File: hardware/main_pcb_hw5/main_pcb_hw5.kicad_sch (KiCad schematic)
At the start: 27 parts, among them J1 MEGA TOP, J10 GBA_Slot, J2 MEGA BOTTOM, J3 CART SLOT TOP ROW, J4 CART SLOT BOTTOM ROW, J5 MEGA SIDE, J6 5V USB, J7 Conn_01x07, J8 EXP2, J9 EXP1, M2_1 Screw_Terminal_01x01, M2_2 Screw_Terminal_01x01, M2_3 Screw_Terminal_01x01, M2_4 Screw_Terminal_01x01, M2_5 Screw_Terminal_01x01, M2_6 Screw_Terminal_01x01, M2_7 Screw_Terminal_01x01, M2_8 Screw_Terminal_01x01, M2_9 Screw_Terminal_01x01, SW1 VOLTAGE, SW2 POWER

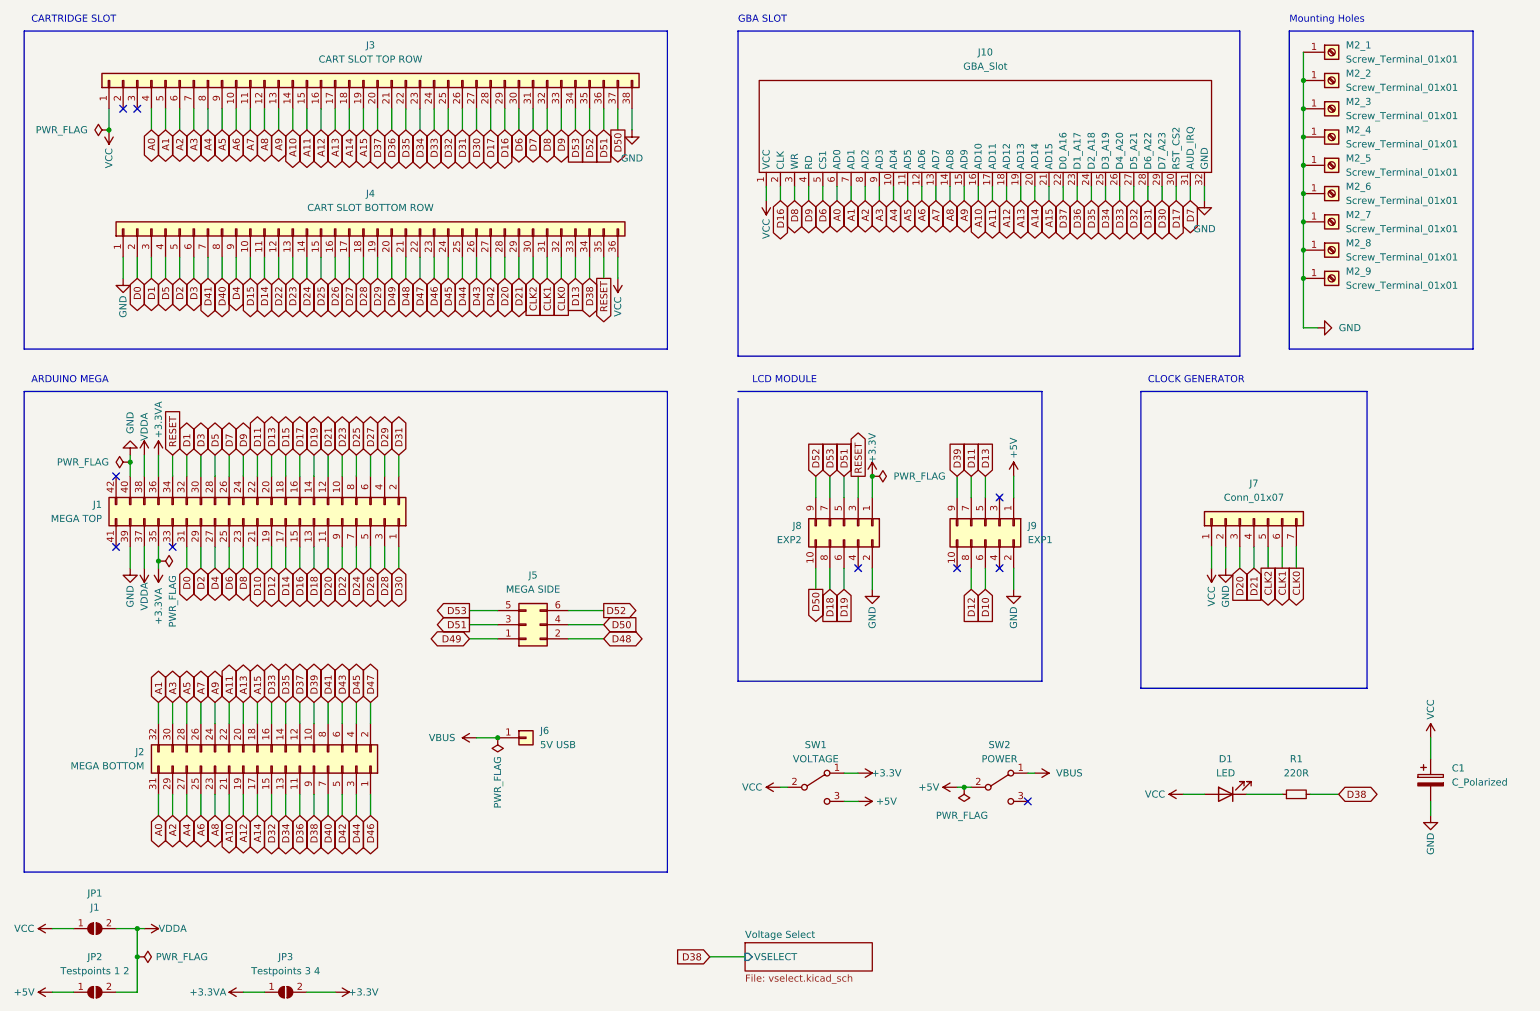
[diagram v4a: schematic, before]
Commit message: HW5 Main PCB, Revision 5
* Migrated files to KiCad 7
* Added RTC
  * IC: Analog Devices Inc. DS3231MZ
  * Battery holder (CR1616): Keystone Electronics 3012
* Cleaned up traces
* Changed ground fill to solid
* Removed test pads and LCD solder jumper
* Cleaned up/prettified silkscreen and logo
* Cleaned up some footprints (more to come eventually)
* Added 3D models for board display
* Schematic image is now a PDF since it has 2 pages
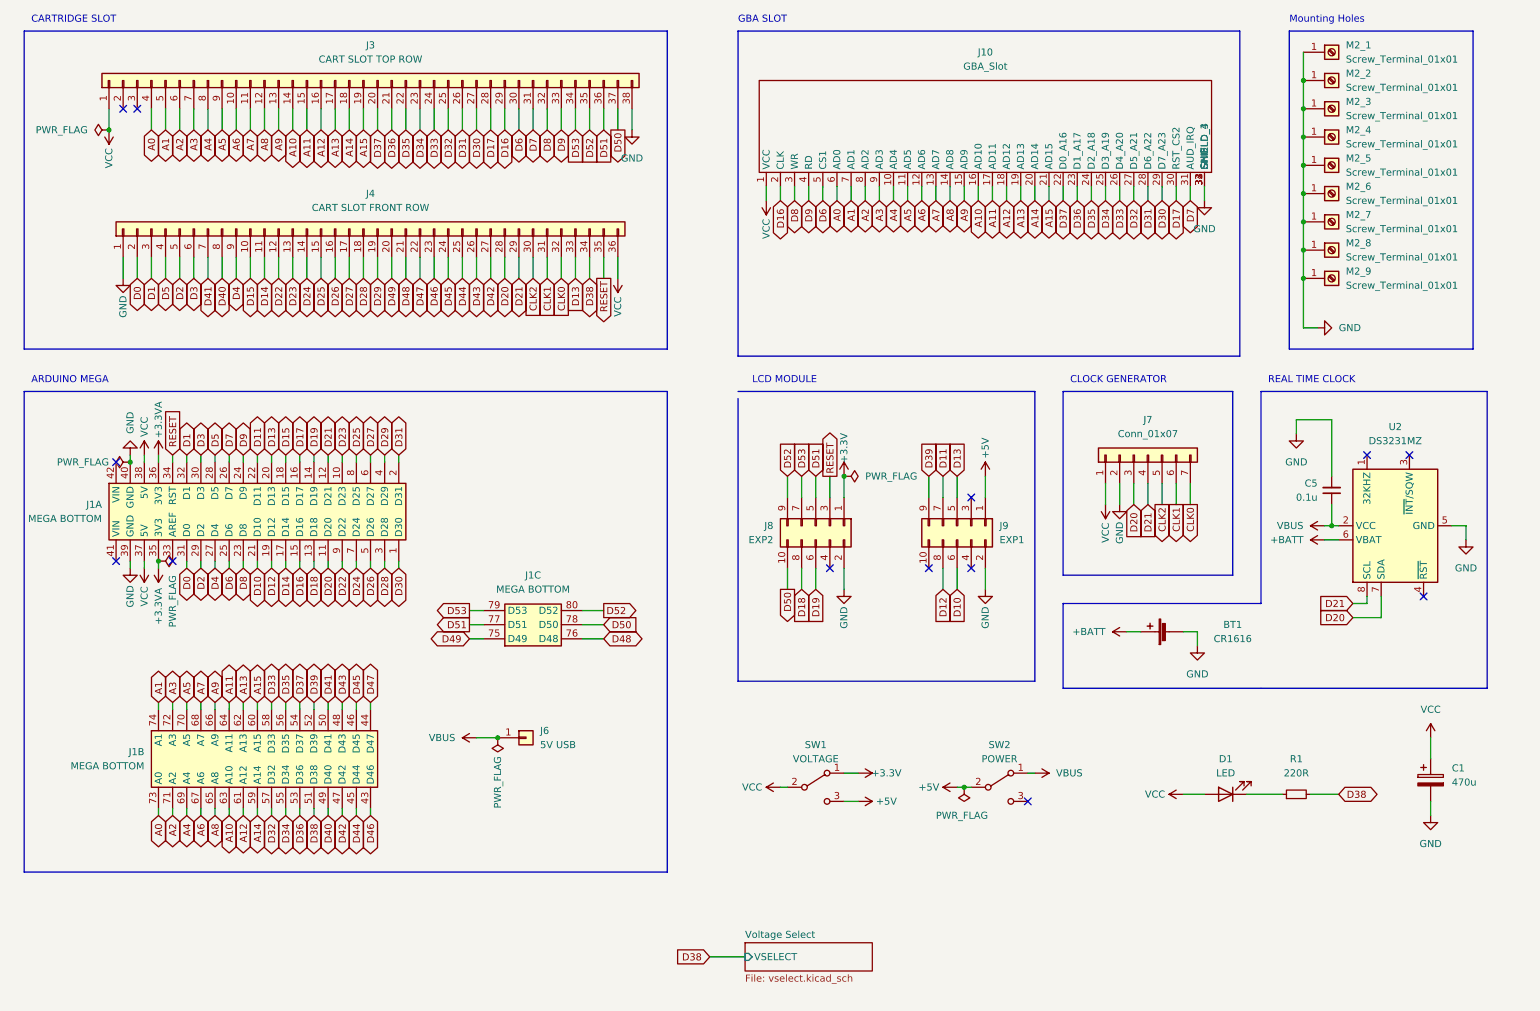
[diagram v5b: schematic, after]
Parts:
- removed JP1: J1, symbol Jumper:SolderJumper_2_Open
- removed JP2: Testpoints 1 2, symbol Jumper:SolderJumper_2_Open
- removed JP3: Testpoints 3 4, symbol Jumper:SolderJumper_2_Open
- added BT1: CR1616, !OSCR:CR1616, symbol Device:Battery_Cell
- added C5: 0.1u, Capacitor_SMD:C_0402_1005Metric_Pad0.74x0.62mm_HandSolder, symbol Device:C_Small
- added U2: DS3231MZ, Package_SO:SOIC-8_3.9x4.9mm_P1.27mm, symbol Timer_RTC:DS3231MZ
- C1: value C_Polarized -> 470u; footprint (none) -> Capacitor_THT:CP_Radial_D8.0mm_P3.50mm
- D1: footprint (none) -> LED_THT:LED_D3.0mm
- J1: renamed from J5; value MEGA SIDE -> MEGA BOTTOM; footprint Connector_PinSocket_2.54mm:PinSocket_2x03_P2.54mm_Vertical -> !OSCR:MEGA2560_PRO_MINI; symbol Connector_Generic:Conn_02x03_Odd_Even -> !OSCR:MEGA2650_PRO_MINI
- J1: renamed from J2; footprint Connector_PinSocket_2.54mm:PinSocket_2x16_P2.54mm_Vertical -> !OSCR:MEGA2560_PRO_MINI; symbol Connector_Generic:Conn_02x16_Odd_Even -> !OSCR:MEGA2650_PRO_MINI
- J1: value MEGA TOP -> MEGA BOTTOM; footprint Connector_PinSocket_2.54mm:PinSocket_2x21_P2.54mm_Vertical -> !OSCR:MEGA2560_PRO_MINI; symbol Connector_Generic:Conn_02x21_Odd_Even -> !OSCR:MEGA2650_PRO_MINI
- J3: footprint Connector_PinSocket_2.54mm:PinSocket_1x38_P2.54mm_Vertical -> !OSCR:Cartridge_Port_Adapter-Back
- J4: value CART SLOT BOTTOM ROW -> CART SLOT FRONT ROW; footprint Connector_PinSocket_2.54mm:PinSocket_1x36_P2.54mm_Vertical -> !OSCR:Cartridge_Port_Adapter-Front
- J7: footprint (none) -> !OSCR:Clock_Generator_Header
- J8, J9: footprint Connector_IDC:IDC-Header_2x05_P2.54mm_Vertical -> !OSCR:LCD_Header
- R1: footprint (none) -> Resistor_THT:R_Axial_DIN0207_L6.3mm_D2.5mm_P10.16mm_Horizontal
- SW1, SW2: footprint (none) -> !OSCR:Power_Switch
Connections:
- net VDDA is gone; now on net VCC: J1.37 (5V), J1.38 (5V)
- net A0: now also J1.73 (A0); no longer J1.31 (Pin_31)
- net A1: now also J1.74 (A1); no longer J1.32 (Pin_32)
- net A10: now also J1.63 (A10); no longer J1.21 (Pin_21)
- net A11: now also J1.64 (A11); no longer J1.22 (Pin_22)
- net A12: now also J1.61 (A12); no longer J1.19 (Pin_19)
- net A13: now also J1.62 (A13); no longer J1.20 (Pin_20)
- net A14: now also J1.59 (A14); no longer J1.17 (Pin_17)
- net A15: now also J1.60 (A15); no longer J1.18 (Pin_18)
- net A2: now also J1.71 (A2); no longer J1.29 (Pin_29)
- net A3: now also J1.72 (A3); no longer J1.30 (Pin_30)
- net A4: now also J1.69 (A4); no longer J1.27 (Pin_27)
- net A5: now also J1.70 (A5); no longer J1.28 (Pin_28)
- net A6: now also J1.67 (A6); no longer J1.25 (Pin_25)
- net A7: now also J1.68 (A7); no longer J1.26 (Pin_26)
- net A8: now also J1.65 (A8); no longer J1.23 (Pin_23)
- net A9: now also J1.66 (A9); no longer J1.24 (Pin_24)
- net D20: now also U2.7 (SDA)
- net D21: now also U2.8 (SCL)
- net D32: now also J1.57 (D32); no longer J1.15 (Pin_15)
- net D33: now also J1.58 (D33); no longer J1.16 (Pin_16)
- net D34: now also J1.55 (D34); no longer J1.13 (Pin_13)
- net D35: now also J1.56 (D35); no longer J1.14 (Pin_14)
- net D36: now also J1.53 (D36); no longer J1.11 (Pin_11)
- net D37: now also J1.54 (D37); no longer J1.12 (Pin_12)
- net D38: now also J1.51 (D38); no longer J1.9 (Pin_9)
- net D39: now also J1.52 (D39); no longer J1.10 (Pin_10)
- net D40: now also J1.49 (D40); no longer J1.7 (Pin_7)
- net D41: now also J1.50 (D41); no longer J1.8 (Pin_8)
- net D42: now also J1.47 (D42); no longer J1.5 (Pin_5)
- net D43: now also J1.48 (D43); no longer J1.6 (Pin_6)
- net D44: now also J1.45 (D44); no longer J1.3 (Pin_3)
- net D45: now also J1.46 (D45); no longer J1.4 (Pin_4)
- net D46: now also J1.43 (D46); no longer J1.1 (Pin_1)
- net D47: now also J1.44 (D47); no longer J1.2 (Pin_2)
- net D48: now also J1.76 (D48); no longer J1.2 (Pin_2)
- net D49: now also J1.75 (D49); no longer J1.1 (Pin_1)
- net D50: now also J1.78 (D50); no longer J1.4 (Pin_4)
- net D51: now also J1.77 (D51); no longer J1.3 (Pin_3)
- net D52: now also J1.80 (D52); no longer J1.6 (Pin_6)
- net D53: now also J1.79 (D53); no longer J1.5 (Pin_5)
- net GND: now also J10.33 (SHIELD_3), J10.34 (SHIELD_4), BT1.2 (-), C5.2, U2.5 (GND)
- net VBUS: now also C5.1, U2.2 (VCC)
- new net +BATT: BT1.1 (+), U2.6 (VBAT)
- no-connect marks 10 -> 13
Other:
- note added: "REAL TIME CLOCK"
- moved on the sheet: J1A, J1B, J7, J8, J9
